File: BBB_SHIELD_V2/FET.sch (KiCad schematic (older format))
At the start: 15 parts, among them J6 Screw_Terminal_01x02, Q1 Q_NMOS_GDS, U6 TLV333

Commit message: Changed to high-side switching of power supply to boards.  Changed footprints to SOIC.  Misc other changes.
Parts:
- removed D8: D_ALT, CUSTOM_FOOTPRINTS:DO-221AC, symbol Device:D_ALT
- removed D9: BAS70-04, Package_TO_SOT_SMD:SOT-23, symbol Device:D_Schottky_x2_Serial_AKC
- removed J6: Screw_Terminal_01x02, CUSTOM_FOOTPRINTS:OSTTA024163, symbol Connector:Screw_Terminal_01x02
- removed R18: 100R 1%, Resistor_SMD:R_0805_2012Metric, symbol Device:R
- removed R19: 1K5 1%, Resistor_SMD:R_0805_2012Metric, symbol CUSTOM_COMPONENTS:R_C
- removed R20: 4K7 1%, Resistor_SMD:R_0805_2012Metric, symbol CUSTOM_COMPONENTS:R_C
- removed TP7, TP8, TP9: TestPoint_2Pole, Connector_PinHeader_1.27mm:PinHeader_1x02_P1.27mm_Vertical, symbol Connector:TestPoint_2Pole
- removed U6: TLV333, Package_SO:SOIC-8_3.9x4.9mm_P1.27mm, symbol CUSTOM_COMPONENTS:TLV333
- added D10, D11, D9: D_ALT, FOOTPRINT:COMCHIP_TO_277, symbol Device:D_ALT
- added R23: 100R, Resistor_SMD:R_0805_2012Metric, symbol CUSTOM_COMPONENTS:R_C
- added R24: 24K9, Resistor_SMD:R_0805_2012Metric, symbol Device:R
- added TPFETOUT1: TestPoint, TestPoint:TestPoint_THTPad_D1.0mm_Drill0.5mm, symbol Connector:TestPoint
- added TPSHUNT1: TestPoint_2Pole, Connector_PinHeader_1.27mm:PinHeader_1x02_P1.27mm_Vertical, symbol Connector:TestPoint_2Pole
- added U4: INA138, Package_TO_SOT_SMD:SOT-23-5, symbol Amplifier_Current:INA138
- added U5: OPA340NA, Package_TO_SOT_SMD:SOT-23-5, symbol Amplifier_Operational:OPA340NA
- Q1: DKPN (none) -> 1727-4645-ND; MFG (none) -> NXP; NOTES (none) -> BULK, VER 2018-11-25
- R20: renamed from R15; value 100R 1% -> 100R; DKPN (none) -> P16057CT-ND; MFG (none) -> PANASONIC; MFGPN (none) -> ERJ-P06F1000V; NOTES (none) -> CT, VER 2018-11-15
- R21: renamed from R16; value 100R 1% -> 100R; DKPN (none) -> P16057CT-ND; MFG (none) -> PANASONIC; MFGPN (none) -> ERJ-P06F1000V; NOTES (none) -> CT, VER 2018-11-15
- R22: renamed from R17; value 0R2 -> 0.010; footprint Package_TO_SOT_THT:TO-220-2_Vertical -> (none); DKPN (none) -> CFG0612-FX-R010ELFCT-ND; MFG (none) -> BOURNS; MFGPN PWR220T-20-R200F -> CFG0612-FX-R010ELF; NOTES (none) -> BULK
- TP7: renamed from TP6; value TestPoint_2Pole -> TEST_POINT; DKPN (none) -> 952-3598-ND; MFGPN (none) -> M50-3530242; NOTES (none) -> BULK, VER 2018-12-09
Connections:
- net labels added: FET_OUT, _POWER_OUT
- wire segments 43 -> 50
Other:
- note removed: ""R1""
- note removed: ""R2""
- note removed: "A = 1 + R2/R1"
- moved on the sheet: Q1, R20, R21, R22, TP7

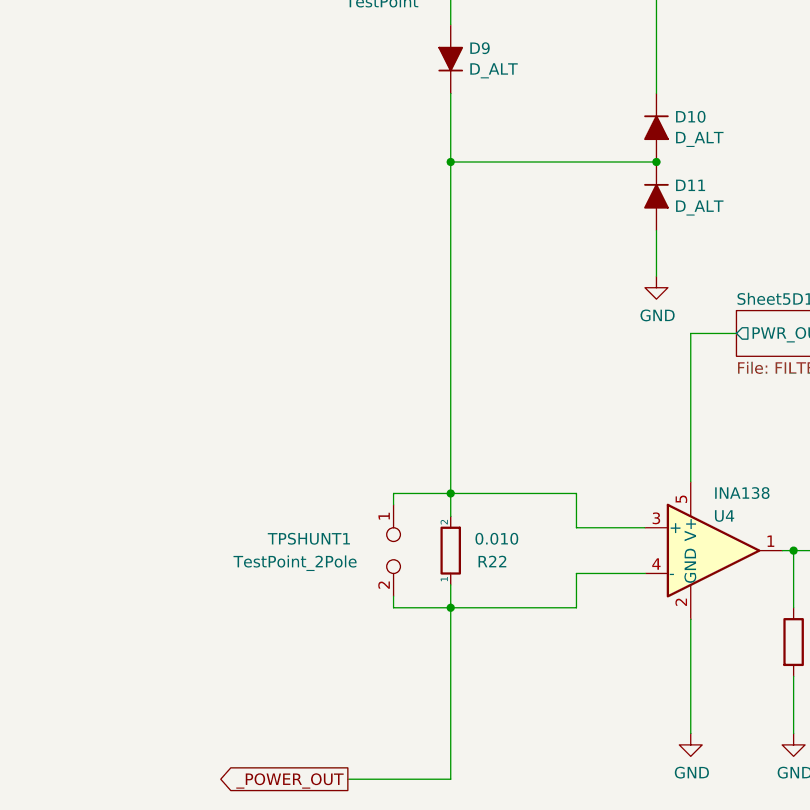
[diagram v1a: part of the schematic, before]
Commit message: Cleaned up schematic.
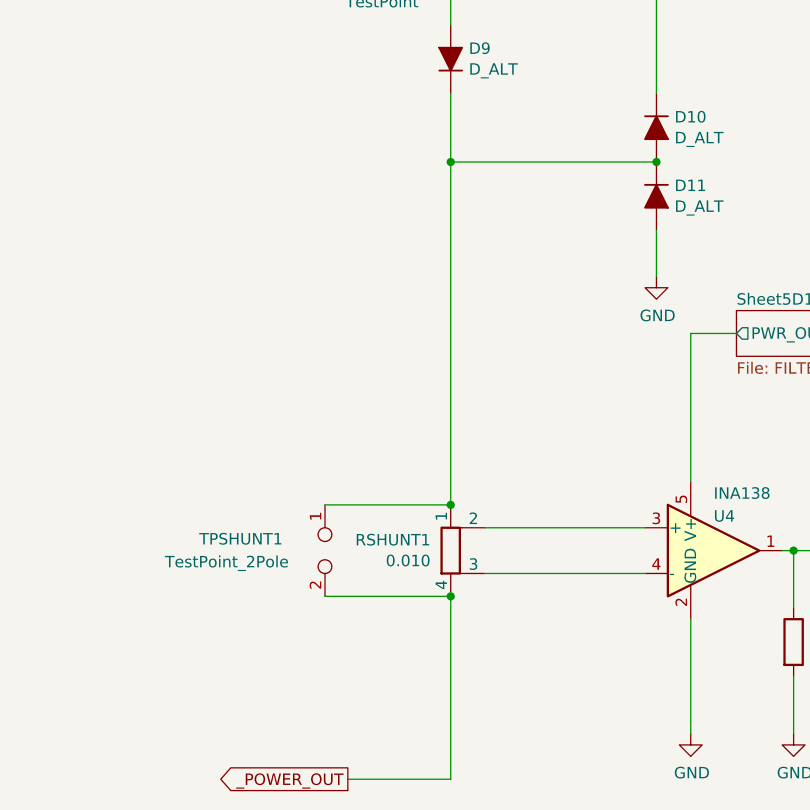
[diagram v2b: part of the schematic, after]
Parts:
- removed R22: 0.010, symbol CUSTOM_COMPONENTS:R_C
- added RSHUNT1: 0.010, CUSTOM_FOOTPRINTS:1206_WIDE_SHUNT, symbol Device:R_Shunt
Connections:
- net _POWER_OUT: now also RSHUNT1.4; no longer U4.4 (-)
- net at D10.2 (A), D11.1 (K), D9.1 (K)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: now also RSHUNT1.1; no longer U4.3 (+)
- new net: RSHUNT1.2, U4.3 (+)
- new net: RSHUNT1.3, U4.4 (-)
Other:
- moved on the sheet: TPSHUNT1
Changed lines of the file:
@@
-$EndComp
-$Comp
-L CUSTOM_COMPONENTS:R_C R22
-U 1 1 5BA135A9
-P 5300 5150
-AR Path="/5BA135A9" Ref="R22"  Part="1"
-AR Path="/5BA13116/5BA135A9" Ref="R22"  Part="1"
-F 0 "R22" H 5050 5200 50  0000 L CNN
-F 1 "0.010" H 5000 5100 50  0000 L CNN
-F 2 "" V 5230 5150 50  0001 C CNN
-F 3 "" H 5300 5150 50  0001 C CNN
-F 4 "CFG0612-FX-R010ELF" H 5300 5150 50  0001 C CNN "MFGPN"
-F 5 "CFG0612-FX-R010ELFCT-ND" H 2000 1050 50  0001 C CNN "DKPN"
-F 6 "BULK" H 2000 1050 50  0001 C CNN "NOTES"
-F 7 "BOURNS" H 2000 1050 50  0001 C CNN "MFG"
-	1    5300 5150
-	-1   0    0    1
 $EndComp
 $Comp
@@
 	6200 3450 5300 3450
 Connection ~ 6200 3450
-Connection ~ 5300 3450
 Wire Wire Line
 	6200 3150 6200 1500
@@
 	1    0    0    -1
 $EndComp
-Wire Wire Line
-	5850 5400 5300 5400
-Wire Wire Line
-	5300 5300 5300 5400
-Connection ~ 5300 5400
-Wire Wire Line
-	5300 4900 5850 4900
-Connection ~ 5300 4900
-Wire Wire Line
-	5300 4900 5300 5000
-Wire Wire Line
-	5300 5400 5300 6150
-Wire Wire Line
-	6150 5050 5850 5050
-Wire Wire Line
-	5850 5250 6150 5250
-Wire Wire Line
-	5850 5250 5850 5400
-Wire Wire Line
-	5850 4900 5850 5050
 Wire Wire Line
 	6750 5150 6800 5150
@@
 Wire Wire Line
 	7450 5550 7450 5950
-Wire Wire Line
-	5300 3450 5300 4900
 $Comp
 L Connector:TestPoint_2Pole TPSHUNT1
 U 1 1 5D13BBC8
-P 5050 5150
-F 0 "TPSHUNT1" V 5000 4600 50  0000 L CNN
-F 1 "TestPoint_2Pole" V 5100 4450 50  0000 L CNN
-F 2 "Connector_PinHeader_1.27mm:PinHeader_1x02_P1.27mm_Vertical" H 5050 5150 50  0001 C CNN
-F 3 "~" H 5050 5150 50  0001 C CNN
-	1    5050 5150
-	0    1    1    0
-$EndComp
-Wire Wire Line
-	5050 4950 5050 4900
-Wire Wire Line
-	5050 4900 5300 4900
-Wire Wire Line
-	5050 5350 5050 5400
-Wire Wire Line
-	5050 5400 5300 5400
+P 4750 5150
+F 0 "TPSHUNT1" V 4700 4600 50  0000 L CNN
+F 1 "TestPoint_2Pole" V 4800 4450 50  0000 L CNN
+F 2 "Connector_PinHeader_1.27mm:PinHeader_1x02_P1.27mm_Vertical" H 4750 5150 50  0001 C CNN
+F 3 "~" H 4750 5150 50  0001 C CNN
+	1    4750 5150
+	0    1    1    0
+$EndComp
 Wire Wire Line
 	5300 2550 5800 2550
@@
 	0    -1   -1   0
 $EndComp
+$Comp
+L Device:R_Shunt RSHUNT1
+U 1 1 5D101A67
+P 5300 5150
+F 0 "RSHUNT1" H 5212 5196 50  0000 R CNN
+F 1 "0.010" H 5212 5105 50  0000 R CNN
+F 2 "CUSTOM_FOOTPRINTS:1206_WIDE_SHUNT" V 5230 5150 50  0001 C CNN
+F 3 "~" H 5300 5150 50  0001 C CNN
+F 4 "CFG0612-FX-R010ELFCT-ND" H 5300 5150 50  0001 C CNN "DKPN"
+F 5 "CFG0612-FX-R010ELF" H 5300 5150 50  0001 C CNN "MFGPN"
+F 6 "BOURNS" H 5300 5150 50  0001 C CNN "MFG"
+	1    5300 5150
+	1    0    0    -1
+$EndComp
+Wire Wire Line
+	5300 3450 5300 4950
+Connection ~ 5300 3450
+Wire Wire Line
+	5450 5050 6150 5050
+Wire Wire Line
+	5450 5250 6150 5250
+Wire Wire Line
+	5300 5350 5300 6150
+Wire Wire Line
+	4750 4950 5300 4950
+Connection ~ 5300 4950
+Wire Wire Line
+	4750 5350 5300 5350
+Connection ~ 5300 5350
 $EndSCHEMATC

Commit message: Schematic cleanup and refinement.
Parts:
- added C45: C, Capacitor_SMD:C_0805_2012Metric, symbol Device:C
- D10, D11, D9: footprint FOOTPRINT:COMCHIP_TO_277 -> CUSTOM_FOOTPRINTS:COMCHIP_TO_277
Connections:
- net GND: now also C45.2
- net I_SENSE: now also C45.1
- net _POWER_OUT: no longer TPSHUNT1.2
- net at D10.2 (A), D11.1 (K), D9.1 (K)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: no longer TPSHUNT1.1
- net I_SENSE_P: now reaches RSHUNT1.2, U4.3 (+)
- net I_SENSE_P: now also TPSHUNT1.1
- net I_SENSE_N: now reaches RSHUNT1.3, U4.4 (-)
- net I_SENSE_N: now also TPSHUNT1.2
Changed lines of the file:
@@
 F 0 "D10" V 6154 3379 50  0000 L CNN
 F 1 "D_ALT" V 6245 3379 50  0000 L CNN
-F 2 "FOOTPRINT:COMCHIP_TO_277" H 6200 3300 50  0001 C CNN
+F 2 "CUSTOM_FOOTPRINTS:COMCHIP_TO_277" H 6200 3300 50  0001 C CNN
 F 3 "~" H 6200 3300 50  0001 C CNN
 F 4 "641-1494-1-ND" V 6200 3300 50  0001 C CNN "DKPN"
@@
 F 0 "D9" V 5346 2921 50  0000 R CNN
 F 1 "D_ALT" V 5255 2921 50  0000 R CNN
-F 2 "FOOTPRINT:COMCHIP_TO_277" H 5300 3000 50  0001 C CNN
+F 2 "CUSTOM_FOOTPRINTS:COMCHIP_TO_277" H 5300 3000 50  0001 C CNN
 F 3 "~" H 5300 3000 50  0001 C CNN
 F 4 "CDBZ310200-HF" V 5300 3000 50  0001 C CNN "MFGPN"
@@
 F 0 "D11" V 6154 3679 50  0000 L CNN
 F 1 "D_ALT" V 6245 3679 50  0000 L CNN
-F 2 "FOOTPRINT:COMCHIP_TO_277" H 6200 3600 50  0001 C CNN
+F 2 "CUSTOM_FOOTPRINTS:COMCHIP_TO_277" H 6200 3600 50  0001 C CNN
 F 3 "~" H 6200 3600 50  0001 C CNN
 F 4 "641-1494-1-ND" V 6200 3600 50  0001 C CNN "DKPN"
@@
 Wire Wire Line
 	6800 5400 6800 5150
-Connection ~ 6800 5150
-Wire Wire Line
-	6800 5150 7250 5150
 $Comp
 L power:GND #PWR038
@@
 Connection ~ 7850 5250
 Wire Wire Line
-	8700 5250 9150 5250
+	8700 5250 8850 5250
 $Comp
 L CUSTOM_COMPONENTS:R_C R23
@@
 Connection ~ 5300 3450
 Wire Wire Line
-	5450 5050 6150 5050
-Wire Wire Line
-	5450 5250 6150 5250
+	5450 5050 5500 5050
+Wire Wire Line
+	5450 5250 5500 5250
 Wire Wire Line
 	5300 5350 5300 6150
 Wire Wire Line
-	4750 4950 5300 4950
-Connection ~ 5300 4950
-Wire Wire Line
-	4750 5350 5300 5350
-Connection ~ 5300 5350
+	5500 4950 5500 5050
+Connection ~ 5500 5050
+Wire Wire Line
+	5500 5050 6150 5050
+Wire Wire Line
+	4750 4950 5500 4950
+Wire Wire Line
+	5500 5350 5500 5250
+Connection ~ 5500 5250
+Wire Wire Line
+	5500 5250 6150 5250
+Wire Wire Line
+	4750 5350 5500 5350
+Text Label 5650 5050 0    50   ~ 0
+I_SENSE_P
+Text Label 5650 5250 0    50   ~ 0
+I_SENSE_N
+Wire Wire Line
+	6800 5150 7250 5150
+Connection ~ 6800 5150
+$Comp
+L Device:C C45
+U 1 1 5D20E77E
+P 8850 5400
+F 0 "C45" H 8965 5446 50  0000 L CNN
+F 1 "C" H 8965 5355 50  0000 L CNN
+F 2 "Capacitor_SMD:C_0805_2012Metric" H 8888 5250 50  0001 C CNN
+F 3 "~" H 8850 5400 50  0001 C CNN
+	1    8850 5400
+	1    0    0    -1
+$EndComp
+Connection ~ 8850 5250
+Wire Wire Line
+	8850 5250 9150 5250
+$Comp
+L power:GND #PWR02
+U 1 1 5D20E7F3
+P 8850 5950
+F 0 "#PWR02" H 8850 5700 50  0001 C CNN
+F 1 "GND" H 8855 5777 50  0000 C CNN
+F 2 "" H 8850 5950 50  0001 C CNN
+F 3 "" H 8850 5950 50  0001 C CNN
+	1    8850 5950
+	1    0    0    -1
+$EndComp
+Wire Wire Line
+	8850 5950 8850 5550
 $EndSCHEMATC

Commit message: Rev 2 problem fixes.
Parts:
- removed TPFETOUT1: TestPoint, TestPoint:TestPoint_THTPad_D1.0mm_Drill0.5mm, symbol Connector:TestPoint
- added C49: 1uF, Capacitor_SMD:C_0805_2012Metric, symbol Device:C
- added R26: 200, Resistor_SMD:R_0805_2012Metric, symbol Device:R
- C45: value C -> 1uF; DKPN (none) -> 1276-2928-2-ND; MFG (none) -> SAMSUNG; MFGPN (none) -> CL31A225KB9LNNC; NOTES (none) -> VER,2019-07-17,REEL; TEMPCO (none) -> X7R; VOLTAGE (none) -> 50
- D10, D11, D9, RSHUNT1: NOTES (none) -> VER,2019-07-15,CT
- Q1: NOTES BULK, VER 2018-11-25 -> VER,2019-07-15,REUSE
- R20: value 100R -> 4K7; NOTES CT, VER 2018-11-15 -> VER,2019-07-17,CT
- R21: value 100R -> 200R; NOTES CT, VER 2018-11-15 -> VER,2019-07-17,CT
- R23: value 100R -> 1K; DKPN P16057CT-ND -> 541-3977-2-ND; MFG PANASONIC -> VISHAY; MFGPN ERJ-P06F1000V -> CRCW08051K00FKEAC; NOTES CT, VER 2018-11-15 -> VER,2019-07-17,CT
- R24: value 24K9 -> 49K9; DKPN (none) -> 541-49.9KAZCT-ND; MFG (none) -> VISHAY; MFGPN (none) -> CRCW080549K9DHEAP
- TP7: NOTES BULK, VER 2018-12-09 -> (none)
- U4, U5: NOTES (none) -> VER,2019-07-16,CT
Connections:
- net GND: now also C49.2
- net at Q1.1 (G), R20.1, R21.1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: now also R26.1
- new net: C49.1, R26.2
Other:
- moved on the sheet: C45, D10, D11, D9, Q1, R20, R21, R23, R24, RSHUNT1, TP7, TPSHUNT1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

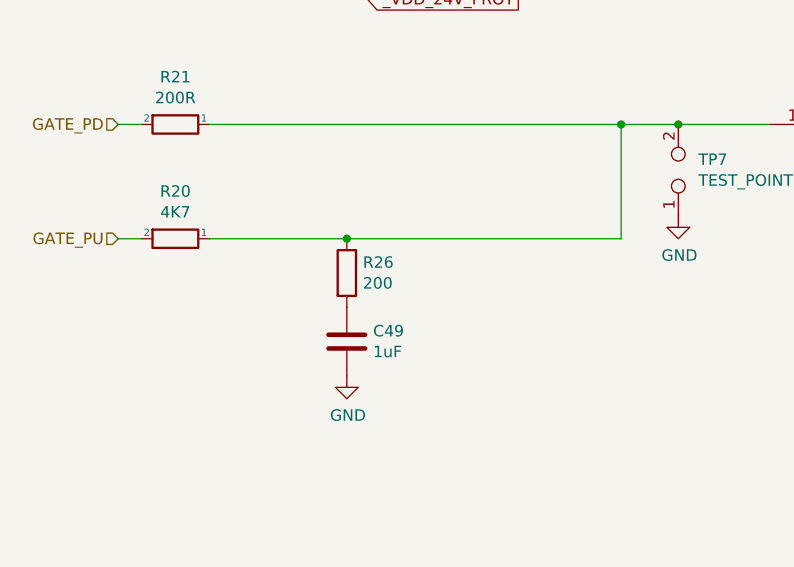
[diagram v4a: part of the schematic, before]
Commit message: Schematics cleanup.  Gerbers for the latest manufacturing release.
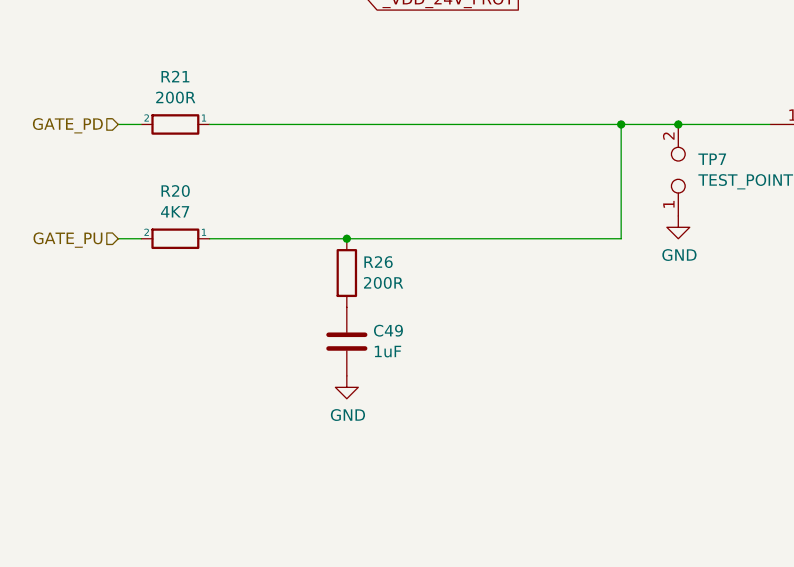
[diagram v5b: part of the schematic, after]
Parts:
- R21: DKPN P16057CT-ND -> 541-4146-1-ND; MFG PANASONIC -> VISHAY; MFGPN ERJ-P06F1000V -> CRCW0805200RFKEAC
- R26: value 200 -> 200R; DKPN (none) -> 541-4146-1-ND; MFG (none) -> VISHAY; MFGPN (none) -> CRCW0805200RFKEAC
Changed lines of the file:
@@
 encoding utf-8
 Sheet 8 12
-Title ""
-Date ""
-Rev ""
-Comp ""
-Comment1 ""
+Title "VPSB"
+Date "2019-09-03"
+Rev "V3.0"
+Comp "Vidas Simkus"
+Comment1 "Copyright (C) 2019 Vidas Simkus"
 Comment2 ""
 Comment3 ""
@@
 F 2 "Resistor_SMD:R_0805_2012Metric" V 1680 1350 50  0001 C CNN
 F 3 "" H 1750 1350 50  0001 C CNN
-F 4 "P16057CT-ND" H -100 -2100 50  0001 C CNN "DKPN"
-F 5 "PANASONIC" H -100 -2100 50  0001 C CNN "MFG"
-F 6 "ERJ-P06F1000V" H -100 -2100 50  0001 C CNN "MFGPN"
+F 4 "541-4146-1-ND" H -100 -2100 50  0001 C CNN "DKPN"
+F 5 "VISHAY" H -100 -2100 50  0001 C CNN "MFG"
+F 6 "CRCW0805200RFKEAC" H -100 -2100 50  0001 C CNN "MFGPN"
 F 7 "VER,2019-07-17,CT" H -100 -2100 50  0001 C CNN "NOTES"
 	1    1750 1350
@@
 P 2500 2000
 F 0 "R26" H 2570 2046 50  0000 L CNN
-F 1 "200" H 2570 1955 50  0000 L CNN
+F 1 "200R" H 2570 1955 50  0000 L CNN
 F 2 "Resistor_SMD:R_0805_2012Metric" V 2430 2000 50  0001 C CNN
-F 3 "~" H 2500 2000 50  0001 C CNN
+F 3 "" H 2500 2000 50  0001 C CNN
+F 4 "541-4146-1-ND" H 0   0   50  0001 C CNN "DKPN"
+F 5 "VISHAY" H 0   0   50  0001 C CNN "MFG"
+F 6 "CRCW0805200RFKEAC" H 0   0   50  0001 C CNN "MFGPN"
 	1    2500 2000
 	1    0    0    -1
